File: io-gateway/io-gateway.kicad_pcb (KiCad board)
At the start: 4 copper layers, 155 x 81.5 mm, 150 parts, among them J1 1752201, J2 1752201, J3 1752201, J4 Screw_Terminal_01x09, J5 Screw_Terminal_01x09, J6 Screw_Terminal_01x09, K1 2071556-2, K2 2071556-2, K3 2071556-2, K4 2071556-2, K5 2071556-2, K6 2071556-2, K7 2071556-2, K8 2071556-2, K9 2071556-2, U3 TPS54308

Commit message: upd
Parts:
- added C_DIMA_25: 10µF 50V, Capacitor_SMD:C_1210_3225Metric, B.Cu at (123.2, 93.9)
- added C_DIMA_26: 10µF 50V, Capacitor_SMD:C_1210_3225Metric, B.Cu at (126.7, 93.9)
- added C_DIMA_27: 470pF, Capacitor_SMD:C_0603_1608Metric, F.Cu at (25.3, 70.8)
- added C_DIMA_28: 100nF 50V, Capacitor_SMD:C_0603_1608Metric, B.Cu at (129.4, 93.1)
- added C_DIMA_29: 22pF, Capacitor_SMD:C_0603_1608Metric, F.Cu at (25.3, 75.8)
- added C_DIMA_30: 100nF 50V, Capacitor_SMD:C_0603_1608Metric, B.Cu at (123.7, 82.2)
- added C_DIMA_31: 1µF 50V, Capacitor_SMD:C_1206_3216Metric, B.Cu at (167.5, 117.0)
- added C_DIMA_32: NM, Capacitor_SMD:C_1206_3216Metric, F.Cu at (35.8, 83.3)
- added C_DIMA_33: 10µF 50V, Capacitor_SMD:C_1210_3225Metric, F.Cu at (-40.4, 100.7)
- added C_DIMA_34: 10µF 50V, Capacitor_SMD:C_1210_3225Metric, F.Cu at (-40.4, 104.9)
- added C_DIMA_35: 470pF, Capacitor_SMD:C_0603_1608Metric, F.Cu at (-41.2, 116.8)
- added C_DIMA_36: 100nF 50V, Capacitor_SMD:C_0603_1608Metric, F.Cu at (-41.2, 119.3)
- added C_DIMA_37: 22pF, Capacitor_SMD:C_0603_1608Metric, F.Cu at (-41.2, 121.8)
- added C_DIMA_38: 100nF 50V, Capacitor_SMD:C_0603_1608Metric, F.Cu at (-41.2, 124.3)
- added C_DIMA_39: 1µF 50V, Capacitor_SMD:C_1206_3216Metric, F.Cu at (-34.7, 100.2)
- added C_DIMA_40: NM, Capacitor_SMD:C_1206_3216Metric, F.Cu at (-34.7, 103.6)
- added C_DIMB_25: 10µF 50V, Capacitor_SMD:C_1210_3225Metric, B.Cu at (174.0, 97.3)
- added C_DIMB_26: 10µF 50V, Capacitor_SMD:C_1210_3225Metric, F.Cu at (165.9, 96.9)
- added C_DIMB_27: 470pF, Capacitor_SMD:C_0603_1608Metric, F.Cu at (-8.67, 80.3)
- added C_DIMB_28: 100nF 50V, Capacitor_SMD:C_0603_1608Metric, F.Cu at (25.3, 78.3)
- added C_DIMB_29: 22pF, Capacitor_SMD:C_0603_1608Metric, F.Cu at (25.3, 80.8)
- added C_DIMB_30: 100nF 50V, Capacitor_SMD:C_0603_1608Metric, F.Cu at (25.3, 83.3)
- added C_DIMB_31: 1µF 50V, Capacitor_SMD:C_1206_3216Metric, F.Cu at (35.8, 86.7)
- added C_DIMB_32: NM, Capacitor_SMD:C_1206_3216Metric, F.Cu at (-6.21, 73.8)
- added C_DIMB_33: 10µF 50V, Capacitor_SMD:C_1210_3225Metric, F.Cu at (-40.4, 109.2)
- added C_DIMB_34: 10µF 50V, Capacitor_SMD:C_1210_3225Metric, F.Cu at (-40.4, 113.4)
- added C_DIMB_35: 470pF, Capacitor_SMD:C_0603_1608Metric, F.Cu at (-37.2, 116.8)
- added C_DIMB_36: 100nF 50V, Capacitor_SMD:C_0603_1608Metric, F.Cu at (-37.2, 119.3)
- added C_DIMB_37: 22pF, Capacitor_SMD:C_0603_1608Metric, F.Cu at (-37.2, 121.8)
- added C_DIMB_38: 100nF 50V, Capacitor_SMD:C_0603_1608Metric, F.Cu at (-37.2, 124.3)
- added C_DIMB_39: 1µF 50V, Capacitor_SMD:C_1206_3216Metric, F.Cu at (-34.7, 106.9)
- added C_DIMB_40: NM, Capacitor_SMD:C_1206_3216Metric, F.Cu at (-34.7, 110.3)
- added D_DIMA_10: D_Zener, Diode_SMD:D_SOD-123, F.Cu at (-40.3, 127.3)
- added D_DIMA_7: D_Schottky, Diode_SMD:D_SMB, F.Cu at (111.5, 68.7)
- added D_DIMA_8: D_Zener, Diode_SMD:D_SOD-123, F.Cu at (115.3, 88.9)
- added D_DIMA_9: D_Schottky, Diode_SMD:D_SMB, F.Cu at (-27.0, 118.3)
- added D_DIMB_10: D_Zener, Diode_SMD:D_SOD-123, F.Cu at (-40.3, 130.6)
- added D_DIMB_7: D_Schottky, Diode_SMD:D_SMB, F.Cu at (1.56, 87.4)
- added D_DIMB_8: D_Zener, Diode_SMD:D_SOD-123, F.Cu at (-11.8, 94.1)
- added D_DIMB_9: D_Schottky, Diode_SMD:D_SMB, F.Cu at (-27.0, 123.9)
- added L_DIMA_4: 47µH 3.8A, Inductor_SMD:L_12x12mm_H8mm, F.Cu at (112.6, 79.6)
- added L_DIMA_5: 47µH 3.8A, Inductor_SMD:L_12x12mm_H8mm, F.Cu at (194.7, 87.5)
- added L_DIMB_4: 47µH 3.8A, Inductor_SMD:L_12x12mm_H8mm, F.Cu at (153.2, 79.2)
- added L_DIMB_5: 47µH 3.8A, Inductor_SMD:L_12x12mm_H8mm, F.Cu at (194.7, 103.3)
- added RS_DIMA_4: R, Resistor_SMD:R_1206_3216Metric, B.Cu at (172.5, 115.7)
- added RS_DIMA_5: R, Resistor_SMD:R_1206_3216Metric, F.Cu at (-34.6, 127.2)
- added RS_DIMB_4: R, Resistor_SMD:R_1206_3216Metric, F.Cu at (30.1, 83.9)
- added RS_DIMB_5: R, Resistor_SMD:R_1206_3216Metric, F.Cu at (-34.6, 130.6)
- added R_DIMA_10: 47k, Resistor_SMD:R_0603_1608Metric, F.Cu at (-33.2, 119.3)
- added R_DIMA_7: 24k9, Resistor_SMD:R_0603_1608Metric, F.Cu at (-4.66, 80.3)
- added R_DIMA_8: 47k, Resistor_SMD:R_0603_1608Metric, B.Cu at (135.1, 87.6)
- added R_DIMA_9: 24k9, Resistor_SMD:R_0603_1608Metric, F.Cu at (-33.2, 116.8)
- added R_DIMB_10: 47k, Resistor_SMD:R_0603_1608Metric, F.Cu at (-33.2, 124.3)
- added R_DIMB_7: 24k9, Resistor_SMD:R_0603_1608Metric, F.Cu at (-4.66, 85.4)
- added R_DIMB_8: 47k, Resistor_SMD:R_0603_1608Metric, F.Cu at (25.3, 88.3)
- added R_DIMB_9: 24k9, Resistor_SMD:R_0603_1608Metric, F.Cu at (-33.2, 121.8)
- added U_DIMA4: LED5000, Package_SO:HSOP-8-1EP_3.9x4.9mm_P1.27mm_EP2.41x3.1mm, B.Cu at (128.4, 84.8)
- added U_DIMA5: LED5000, Package_SO:HSOP-8-1EP_3.9x4.9mm_P1.27mm_EP2.41x3.1mm, F.Cu at (-27.7, 101.9)
- added U_DIMB4: LED5000, Package_SO:HSOP-8-1EP_3.9x4.9mm_P1.27mm_EP2.41x3.1mm, F.Cu at (31.7, 100.4)
- added U_DIMB5: LED5000, Package_SO:HSOP-8-1EP_3.9x4.9mm_P1.27mm_EP2.41x3.1mm, F.Cu at (-27.7, 108.5)
- C_DIMA_18, D_DIMA_5: moved to B.Cu
- moved K8 289.6 mm to (183.5, 90.4), turned to 90 degrees
- moved K7 285.8 mm to (196.2, 77.6), turned to 90 degrees
- moved K9 260.6 mm to (170.8, 90.4), turned to 90 degrees
- moved K4 131.4 mm to (143.2, 76.5), turned to 90 degrees
- moved K5 110.0 mm to (129.8, 76.5), turned to 90 degrees
- moved C_DIMA_18 4.32 mm to (124.1, 118.1), turned to 180 degrees
- moved C_DIMB_16 4.09 mm to (102.4, 72.8)
- moved D_DIMA_5 3.43 mm to (119.1, 109.2)
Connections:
- J3 pad 1: VIN_DIM3 -> /Dimmer4/VIN_DIM
- J3 pad 2: GND_DIM3 -> GND_CTRL
- J3 pad 7: VIN_DIM5 -> /Dimmer5/VIN_DIM
- J3 pad 8: GND_DIM5 -> GND_CTRL
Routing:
- net /Dimmer4/DIM1_SW: track 0.00 -> 89.8 mm, vias 0 -> 8
- net DIM7_VLED_GND: track 0.00 -> 61.7 mm, vias 0 -> 2
- net DIM7_VLED_VCC: track 0.00 -> 48.6 mm
- net /Relay9/VAC_OUT: track 0.00 -> 30.2 mm
- net /Relay9/VAC_IN: track 0.00 -> 28.5 mm
- net /Relay8/VAC_IN: track 0.00 -> 27.6 mm
- net /Relay8/VAC_OUT: track 0.00 -> 27.0 mm
- net /Dimmer4/DIM1_FB: track 0.00 -> 21.3 mm, vias 0 -> 2
- net /Relay7/VAC_IN: track 0.00 -> 19.0 mm
- net /Relay4/VAC_IN: track 0.00 -> 16.3 mm
- net /Relay5/VAC_IN: track 0.00 -> 14.9 mm
- net /Relay7/VAC_OUT: track 0.00 -> 13.3 mm
- net /Relay5/VAC_OUT: track 0.00 -> 13.0 mm
- net /Relay4/VAC_OUT: track 0.00 -> 12.3 mm
- net /Dimmer4/VIN_DIM: track 0.00 -> 6.28 mm
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- added copper zone on B.Cu, net /Dimmer4/DIM1_SW
- added copper zone on B.Cu, net /Dimmer4/VIN_DIM
- added copper zone on In1.Cu, net /Dimmer4/VIN_DIM
- removed copper zone on B.Cu, net /Dimmer3/DIM1_SW

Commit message: upd
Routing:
- net GND_CTRL: track 202.4 -> 198.9 mm
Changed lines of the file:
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@@
-	)
-	(segment
-		(start 125.411 109.589)
-		(end 125.411 110.478)
-		(width 0.3)
-		(layer "B.Cu")
-		(net 87)
 	)
 	(segment
@@
 	)
 	(segment
-		(start 125.411 110.478)
-		(end 124.522 110.478)
-		(width 0.3)
-		(layer "B.Cu")
-		(net 87)
-	)
-	(segment
 		(start 124.714 84.582)
 		(end 124.714 83.566)
@@
 	)
 	(segment
-		(start 124.522 109.589)
-		(end 125.411 109.589)
-		(width 0.3)
-		(layer "B.Cu")
-		(net 87)
-	)
-	(segment
 		(start 102.6922 74.295001)
 		(end 102.6922 79.0194)
@@
 		(layer "B.Cu")
 		(net 87)
-	)
-	(segment
-		(start 124.522 109.589)
-		(end 124.522 110.478)
-		(width 0.3)
-		(layer "B.Cu")
-		(net 87)

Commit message: all dimmers placed
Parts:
- C_DIMA_27, C_DIMA_29, C_DIMA_32, C_DIMA_33, C_DIMA_34, C_DIMA_35, C_DIMA_36, C_DIMA_37, C_DIMA_38, C_DIMA_40, C_DIMB_26, C_DIMB_27, C_DIMB_28, C_DIMB_29, C_DIMB_30, C_DIMB_32, C_DIMB_33, C_DIMB_34, C_DIMB_35, C_DIMB_36, C_DIMB_37, C_DIMB_38, C_DIMB_40, D_DIMA_10, D_DIMA_9, D_DIMB_9, D_K4, D_K5, D_K6, D_K7, D_K9, Q_K4, Q_K5, Q_K6, Q_K7, Q_K9, RS_DIMA_5, RS_DIMB_4, RS_DIMB_5, R_DIMA_10, R_DIMA_7, R_DIMA_9, R_DIMB_10, R_DIMB_7, R_DIMB_8, R_DIMB_9, R_K4, R_K5, R_K6, R_K7, R_K9, U_DIMA5, U_DIMB4, U_DIMB5: moved to B.Cu
- moved D_K8 286.1 mm to (179.8, 94.4), turned to 180 degrees
- moved Q_K8 276.7 mm to (175.3, 95.4), turned to 90 degrees
- moved D_K7 270.5 mm to (192.3, 77.6), turned to 180 degrees
- moved Q_K7 270.1 mm to (188.6, 73.1), turned to -90 degrees
- moved R_K8 268.8 mm to (172.7, 97.3), turned to 90 degrees
- moved R_K7 266.0 mm to (187.7, 68.8), turned to -90 degrees
- moved D_K9 249.0 mm to (167.0, 90.4), turned to 180 degrees
- moved Q_K9 248.9 mm to (163.2, 86.3), turned to -90 degrees
- moved R_K9 245.1 mm to (162.2, 82.0), turned to -90 degrees
- moved C_DIMA_35 242.2 mm to (200.3, 97.7), turned to -90 degrees
- moved C_DIMA_38 241.9 mm to (197.4, 84.1), turned to 90 degrees
- moved C_DIMA_37 241.0 mm to (198.2, 94.1), turned to -90 degrees
- moved D_K4 240.6 mm to (139.3, 76.5), turned to 180 degrees
- moved C_DIMB_35 239.0 mm to (201.5, 103.6), turned to 90 degrees
- moved C_DIMB_37 237.2 mm to (199.6, 108.7), turned to -90 degrees
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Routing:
- net /Dimmer4/VIN_DIM: track 6.28 -> 96.2 mm, vias 0 -> 11
- net DIM8_VLED_VCC: track 0.00 -> 69.7 mm, vias 0 -> 8
- net DIM8_VLED_GND: track 0.00 -> 59.8 mm, vias 0 -> 2
- net /Dimmer5/VIN_DIM: track 0.00 -> 57.9 mm
- net /Dimmer4/DIM1_SW: track 89.8 -> 33.0 mm, vias 8 -> 3
- net DIM7_VLED_VCC: track 48.6 -> 103.1 mm
- net DIM9_VLED_VCC: track 0.00 -> 46.4 mm, vias 0 -> 3
- net GND_CTRL: track 198.9 -> 228.1 mm, vias 77 -> 97
- net /Dimmer4/DIM2_SW: track 0.00 -> 28.0 mm, vias 0 -> 3
- net DIM10_VLED_VCC: track 0.00 -> 26.9 mm, vias 0 -> 2
- net DIM10_VLED_GND: track 0.00 -> 20.2 mm
- net +24V: track 20.0 -> 36.2 mm
- net /Dimmer3/VIN_DIM: track 51.9 -> 65.4 mm
- net DIM9_VLED_GND: track 0.00 -> 11.7 mm
- net /Dimmer5/DIM1_SW: track 0.00 -> 8.59 mm, vias 0 -> 5
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- added copper zone on B.Cu, net /Dimmer4/DIM2_SW
- added copper zone on B.Cu, net /Dimmer5/DIM1_SW
- added copper zone on F.Cu, net /Dimmer5/DIM1_SW
- added copper zone on B.Cu, net /Dimmer5/DIM2_SW
- added copper zone on F.Cu, net /Dimmer5/DIM2_SW
- added copper zone on B.Cu, net /Dimmer5/VIN_DIM
- added copper zone on F.Cu, net DIM8_VLED_VCC
- added copper zone on In2.Cu, net DIM8_VLED_VCC
- added copper zone on F.Cu, net GND_CTRL

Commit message: upd
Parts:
- C_DIMB_10, C_DIMB_9: moved to F.Cu
- moved C43 108.9 mm to (162.2, 98.4)
- moved C44 108.9 mm to (164.2, 99.2)
- moved L6 108.9 mm to (171.9, 100.4)
- moved R31 108.9 mm to (162.2, 95.6)
- moved R32 108.9 mm to (161.8, 104.8)
- moved R33 108.9 mm to (161.8, 109.1)
- moved C39 108.9 mm to (164.4, 106.6)
- moved U3 108.9 mm to (165.8, 102.9)
- moved C38 108.9 mm to (165.7, 109.1)
- moved C40 108.9 mm to (164.6, 97.9)
- moved C41 108.9 mm to (167.7, 94.4)
- moved C42 108.9 mm to (169.6, 94.4)
- moved R30 108.9 mm to (162.3, 93.4)
- moved R29 99.6 mm to (159.6, 96.6), turned to 90 degrees
- moved R27 99.3 mm to (159.6, 100.5), turned to 90 degrees
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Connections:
- J4 pad 3: unconnected-(J4-Pin_3-Pad3) -> GND_CTRL
- J4 pad 6: unconnected-(J4-Pin_6-Pad6) -> GND_CTRL
- J4 pad 9: unconnected-(J4-Pin_9-Pad9) -> GND_CTRL
- J5 pad 3: unconnected-(J5-Pin_3-Pad3) -> GND_CTRL
- J5 pad 6: unconnected-(J5-Pin_6-Pad6) -> GND_CTRL
- J5 pad 9: unconnected-(J5-Pin_9-Pad9) -> GND_CTRL
- J6 pad 3: unconnected-(J6-Pin_3-Pad3) -> GND_CTRL
- J6 pad 6: unconnected-(J6-Pin_6-Pad6) -> GND_CTRL
- J6 pad 9: unconnected-(J6-Pin_9-Pad9) -> GND_CTRL
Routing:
- net +24V: track 36.2 -> 325.7 mm
- net +5V: track 18.2 -> 63.1 mm
- net /Dimmer2/DIM1_SW: track 16.6 -> 48.8 mm
- net /Dimmer2/VIN_DIM: track 98.0 -> 91.9 mm
- net /MCU_VoltageRegulator/VregFB: track 6.32 -> 12.3 mm
- net Net-(U3-EN): track 15.3 -> 9.33 mm, vias 2 -> 1
- net GND_CTRL: track 228.1 -> 223.1 mm, vias 97 -> 198
- net DIM4_VLED_GND: track 91.4 -> 96.3 mm, vias 7 -> 5
- net DIM7_VLED_GND: track 65.3 -> 62.3 mm, vias 2 -> 3
- net Net-(D_K8-A): track 7.18 -> 9.99 mm
- net Net-(U_DIMB1-COMP): track 6.46 -> 4.33 mm
- net /Relay2/SW_IN: track 1.59 -> 2.92 mm
- net /Dimmer4/VIN_DIM: track 96.2 -> 97.4 mm
- net /VAC_IN_2: track 51.1 -> 49.9 mm
- net /Relay9/VAC_OUT: track 30.2 -> 30.8 mm
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- added copper zone on In2.Cu, net GND_CTRL
- removed copper zone on F.Cu, net +24V

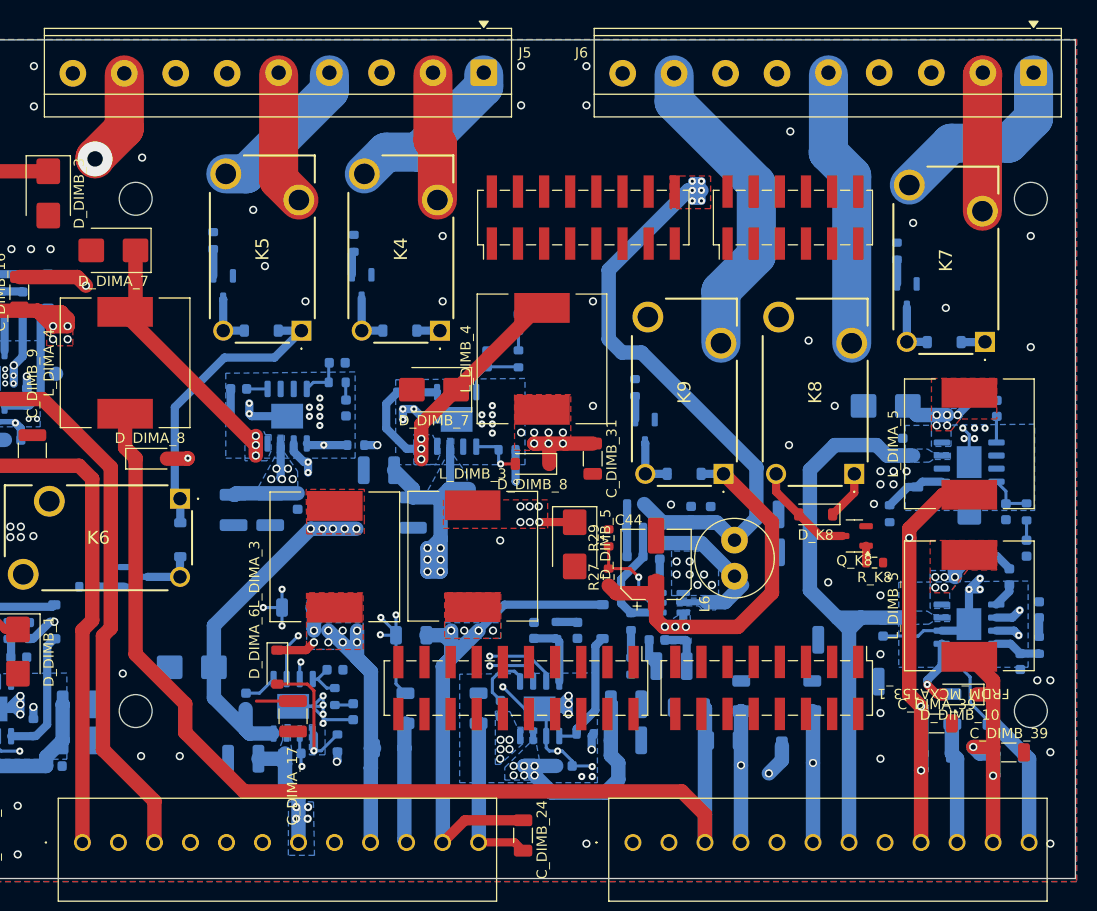
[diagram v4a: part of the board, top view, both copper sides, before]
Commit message: Change Holes to Vias
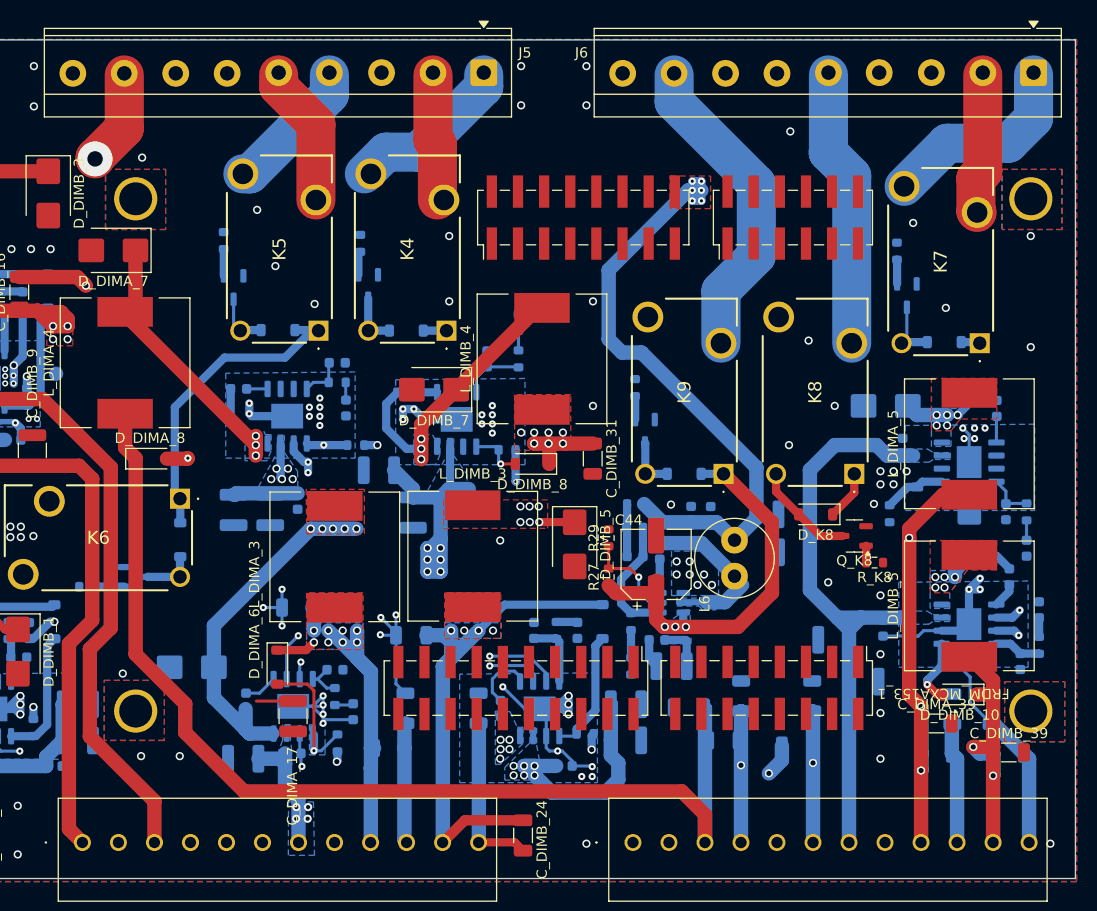
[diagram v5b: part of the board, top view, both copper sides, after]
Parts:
- moved K5 1.66 mm to (131.4, 76.5)
- moved D_K5 1.63 mm to (127.5, 76.5)
- moved R_K5 1.02 mm to (122.2, 67.8)
- moved Q_K5 1.02 mm to (123.2, 72.3)
- moved D_K4 0.63 mm to (140.0, 76.5)
- moved K4 0.63 mm to (143.9, 76.5)
- moved Q_K4 0.63 mm to (136.3, 72.2)
- moved R_K4 0.63 mm to (135.5, 68.0)
- moved K7 0.52 mm to (195.7, 77.7)
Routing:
- net DIM3_VLED_GND: track 83.7 -> 85.4 mm
- net /Relay5/VAC_IN: track 14.9 -> 13.5 mm
- net /Relay6/VAC_IN: track 56.6 -> 57.9 mm
- net /Dimmer2/VIN_DIM: track 91.9 -> 93.0 mm
- net /Relay6/VAC_OUT: track 46.7 -> 47.7 mm
- net DIM3_VLED_VCC: track 83.7 -> 84.7 mm
- net Net-(D_K7-A): track 5.36 -> 6.29 mm
- net /Relay5/VAC_OUT: track 13.0 -> 13.7 mm
- net /Relay7/VAC_IN: track 19.0 -> 19.5 mm
- net GND_CTRL: vias 198 -> 195

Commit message: upd
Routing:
- net /Dimmer3/DIM2_SW: vias 11 -> 10
- net /Dimmer1/VIN_DIM: vias 8 -> 7
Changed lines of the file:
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@@
 	)
 	(via
-		(at 74.916 123.952)
-		(size 0.8)
-		(drill 0.4)
-		(layers "F.Cu" "B.Cu")
-		(net 29)
-	)
-	(via
 		(at 97.1296 118.8212)
 		(size 0.8)
@@
 	)
 	(segment
-		(start 105.9398 80.6976)
-		(end 105.9416 80.6958)
-		(width 1.4)
-		(layer "B.Cu")
-		(net 100)
-	)
-	(segment
 		(start 78.232 90.219)
 		(end 75.0552 90.219)
@@
 	)
 	(segment
-		(start 76.453 78.739)
-		(end 73.533 78.739)
+		(start 76.835 84.963)
+		(end 76.835 79.121)
 		(width 0.3)
 		(layer "F.Cu")
@@
 	)
 	(segment
-		(start 77.089 79.375)
+		(start 77.089 85.217)
+		(end 76.835 84.963)
+		(width 0.3)
+		(layer "F.Cu")
+		(net 112)
+	)
+	(segment
+		(start 76.835 79.121)
 		(end 76.453 78.739)
 		(width 0.3)
@@
 	)
 	(segment
-		(start 77.089 85.217)
-		(end 77.089 79.375)
+		(start 76.453 78.739)
+		(end 73.533 78.739)
 		(width 0.3)
 		(layer "F.Cu")
@@
 	)
 	(via
-		(at 149.098 118.11)
-		(size 0.8)
-		(drill 0.5)
-		(layers "F.Cu" "B.Cu")
-		(free yes)
-		(net 182)
-	)
-	(via
 		(at 151.9794 95.111)
 		(size 0.8)
@@
 		(polygon
 			(pts
-				(xy 150.7602 115.05) (xy 151.319 115.05) (xy 151.319 116.6248) (xy 149.083799 118.6568) (xy 148.6266 118.6568)
+				(xy 150.7602 115.05) (xy 151.319 115.05) (xy 151.319 116.6248) (xy 149.922 117.8948) (xy 148.6266 117.8948)
 				(xy 148.6266 113.4752) (xy 150.049 113.526)
 			)
